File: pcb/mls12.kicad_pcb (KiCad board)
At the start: 4 copper layers, 130 x 40 mm, 137 parts, among them J1 MTJ-88ARX1-FSM-LG, J2 TC2070-FP, J3 SM04B-SRSS-TB, J4 JST B3B-ZR, J5 DC barrel plug, J6 JST B3B-ZR, J7 DC barrel plug, Q1 DMG3406L, Q2 DMG3406L, Q3 DMG3406L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

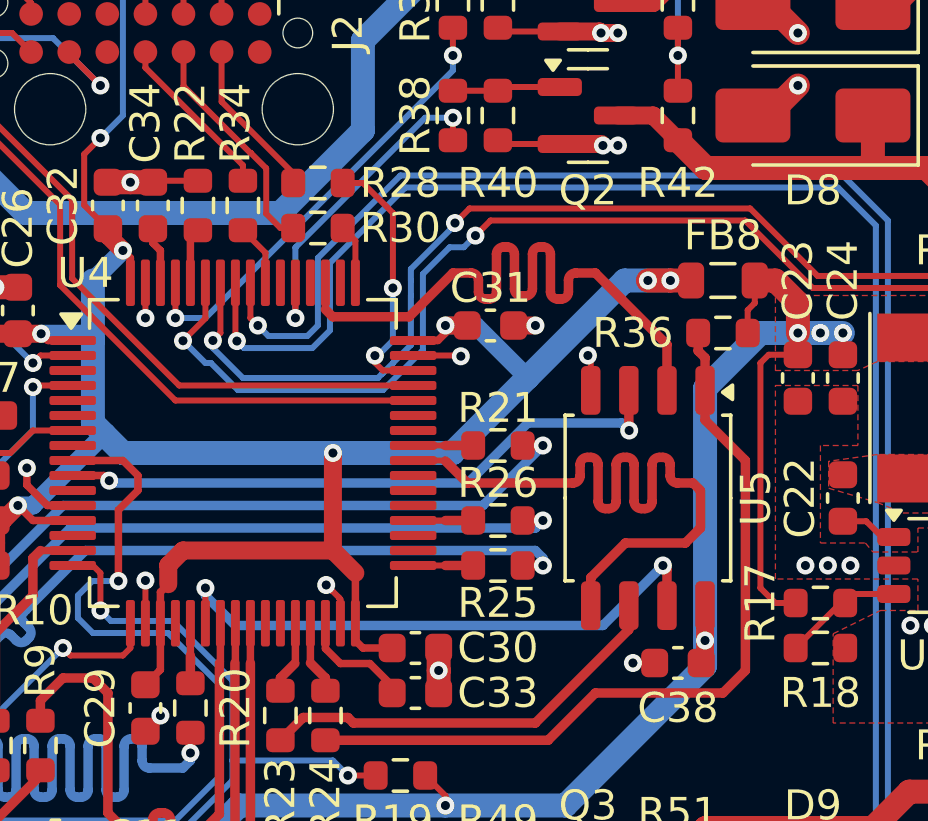
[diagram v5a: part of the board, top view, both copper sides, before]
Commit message: Adjust QSPI length matching
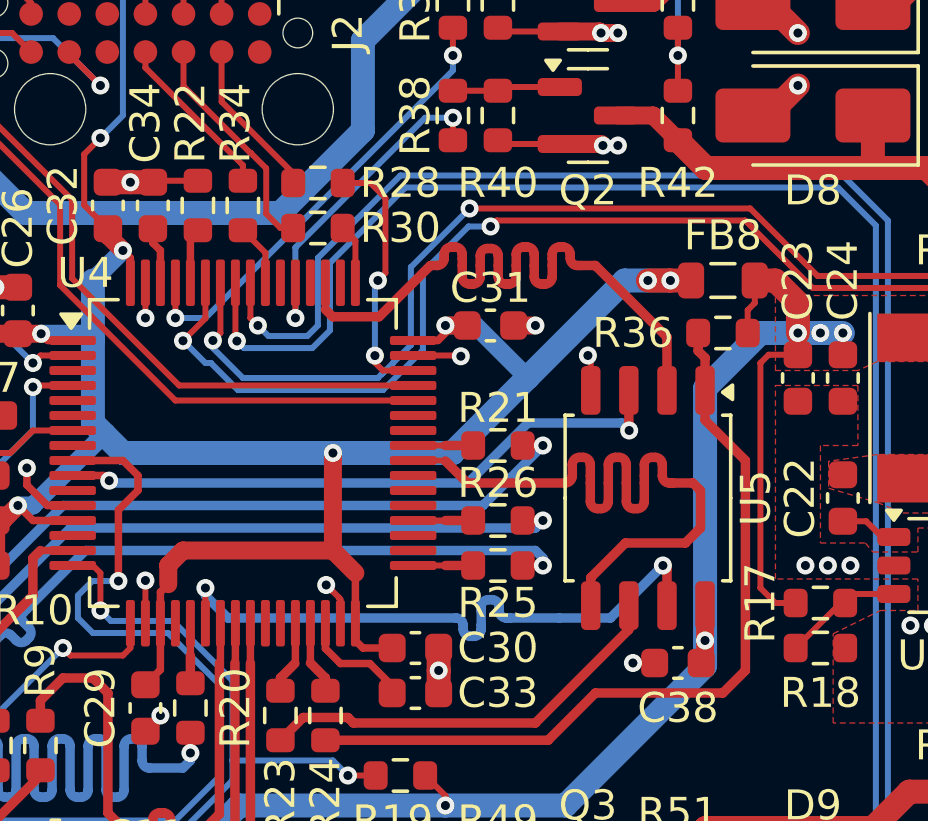
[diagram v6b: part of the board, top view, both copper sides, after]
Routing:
- net /MCU/FLASH.IO_{3}: track 19.3 -> 20.9 mm

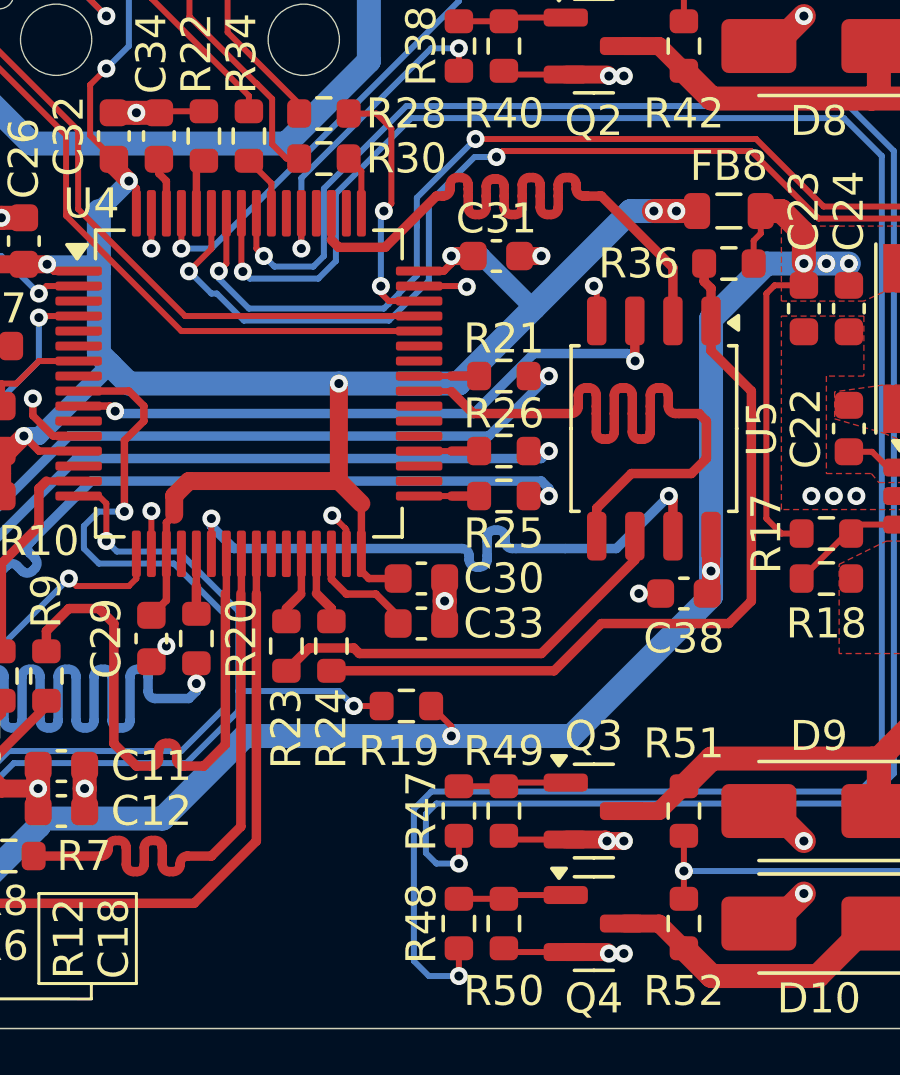
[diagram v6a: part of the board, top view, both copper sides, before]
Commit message: Add blinky LED
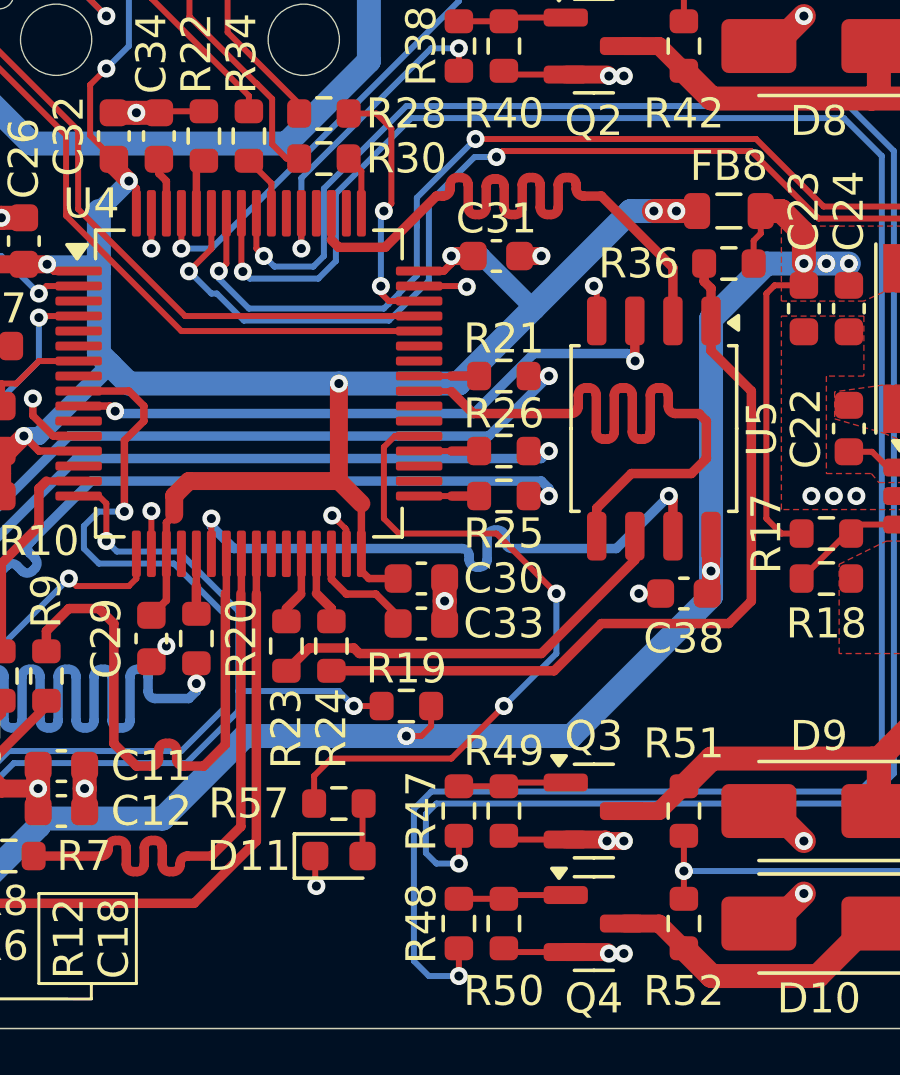
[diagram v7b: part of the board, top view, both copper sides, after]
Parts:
- added D11: Blue, LED_SMD:LED_0603_1608Metric, F.Cu at (195.5, 114.2)
- added R57: 1K, Resistor_SMD:R_0603_1608Metric, F.Cu at (195.5, 112.5)
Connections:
- U4 pad 37: unconnected-(U4C-PC6-Pad37) -> Net-(U4C-PC6)
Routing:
- net Net-(U4C-PC6): track 0.00 -> 23.2 mm, vias 0 -> 2
- net Net-(D11-A): track 0.00 -> 1.77 mm
- net GND: track 73.8 -> 74.8 mm, vias 55 -> 56

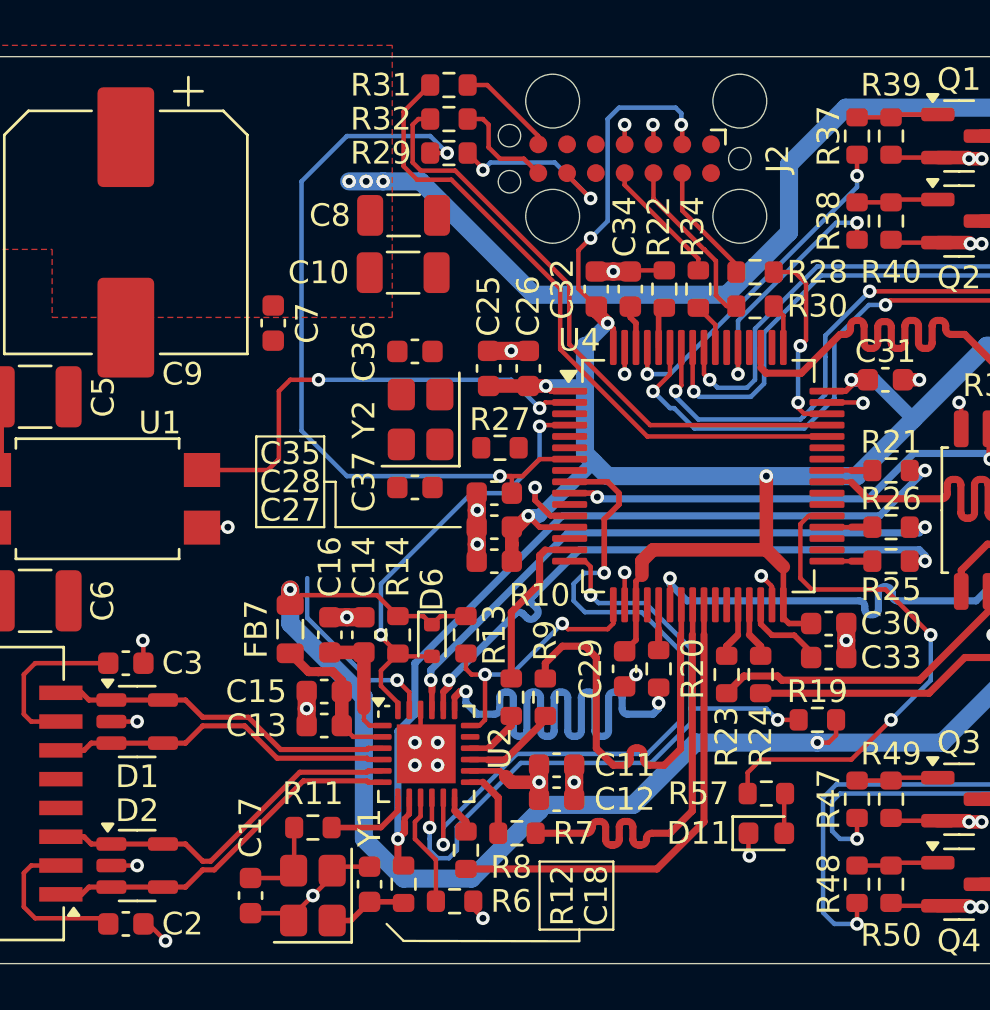
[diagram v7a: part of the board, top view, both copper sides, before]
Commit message: Xtal layout, guard rings
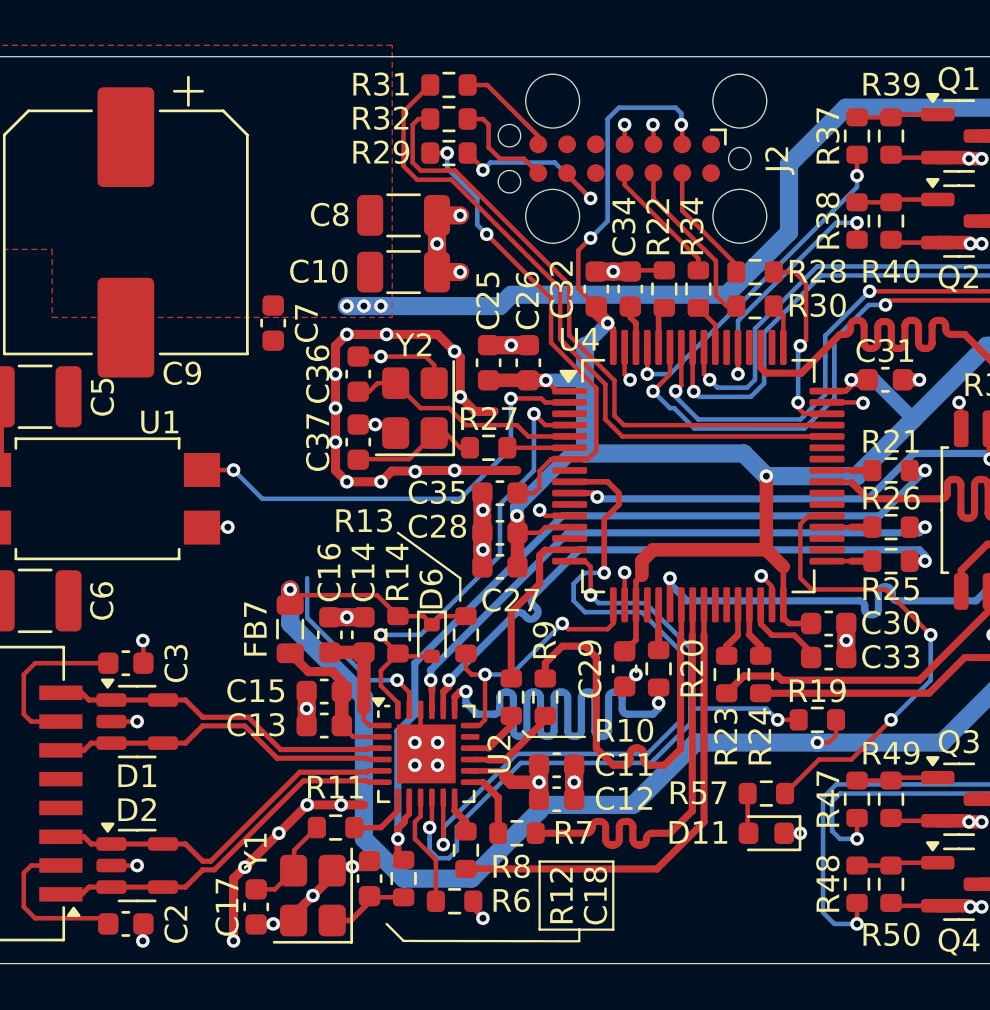
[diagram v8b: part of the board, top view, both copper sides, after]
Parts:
- moved C37 3.20 mm to (177.5, 97.0), turned to -90 degrees
- moved C36 2.69 mm to (177.5, 94.0), turned to 90 degrees
- moved R11 1.00 mm to (176.5, 114.0)
- moved C17 0.56 mm to (173.0, 117.5)
- moved Y2 0.56 mm to (180.0, 95.5)
- moved R27 0.50 mm to (183.2, 97.2)
- moved C27 0.35 mm to (183.8, 102.5)
- moved C28 0.35 mm to (183.8, 101.0)
- moved C18 0.25 mm to (178.0, 116.2)
- moved C25 0.25 mm to (183.2, 93.5)
- moved C26 0.25 mm to (185.0, 93.5)
- moved C35 0.25 mm to (183.8, 99.2)
- moved R12 0.25 mm to (179.5, 116.2)
- turned D11 to 180 degrees
- turned R57 to 180 degrees
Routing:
- net GND: track 74.8 -> 117.0 mm, vias 56 -> 79
- net /MCU/~{RESET}: track 33.8 -> 21.3 mm
- net Net-(U4E-PH0): track 0.00 -> 10.5 mm
- net Net-(C37-Pad2): track 0.00 -> 5.71 mm
- net Net-(U4E-PH1): track 0.00 -> 2.75 mm
- net Net-(U4C-PC6): track 23.2 -> 21.0 mm
- net +24V: track 143.9 -> 142.1 mm
- net /MCU/V_{t,ref}: track 83.2 -> 84.6 mm
- net /ETH-PHY/~{RST}: track 20.1 -> 21.1 mm
- net Net-(U2-XO): track 3.80 -> 2.80 mm
- net /MCU/DBG_UART_TX: track 27.2 -> 27.8 mm
- net /MCU/DBG_UART_RX: track 29.3 -> 29.9 mm
